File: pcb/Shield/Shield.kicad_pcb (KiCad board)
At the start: 2 copper layers, 17.8 x 33 mm, 30 parts, among them J11 TRRS_SJ1-42514, SW1 SW_RST, U1 ATMEGA32U4, X1 XTAL_GND

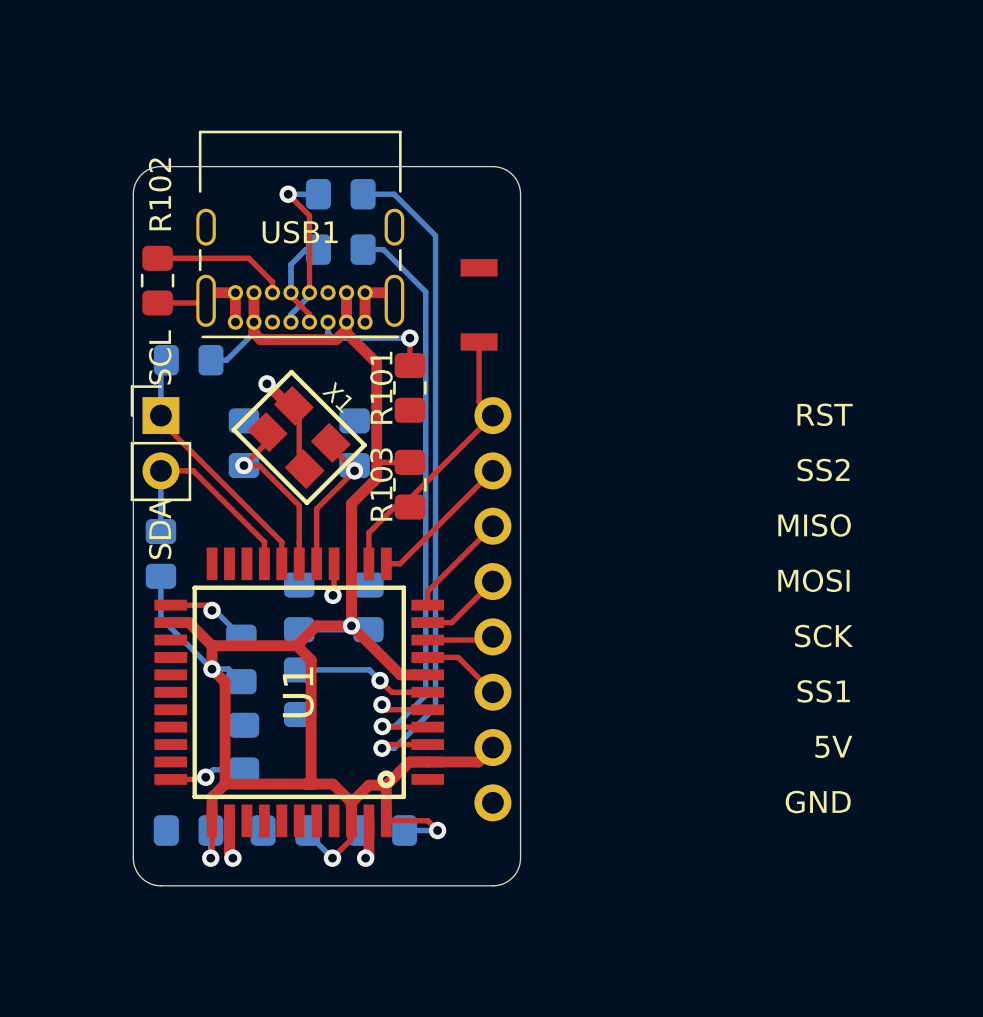
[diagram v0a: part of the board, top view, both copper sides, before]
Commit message: Modified shield to make i2c & usb connections solderless
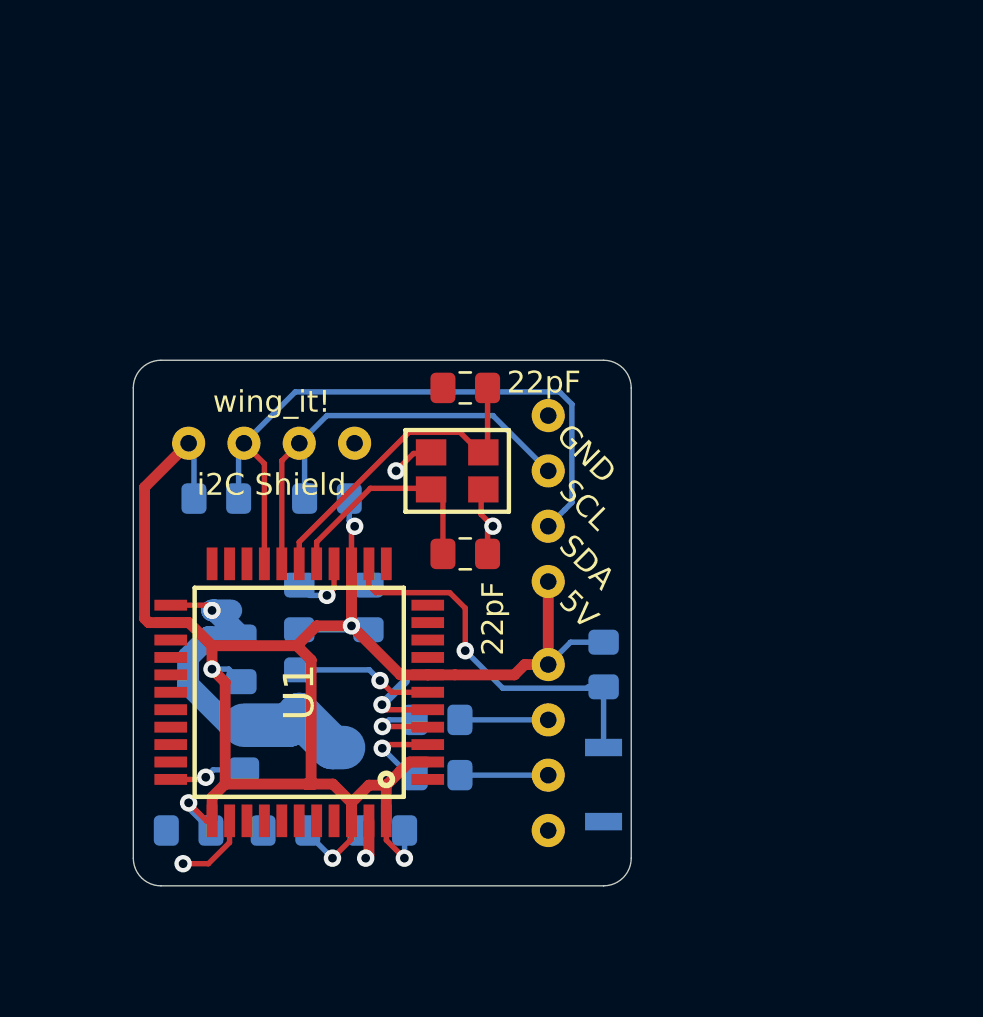
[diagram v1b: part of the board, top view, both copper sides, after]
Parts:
- removed GND, MISO, MOSI, RST, SCK, SS1, SS2, VCC: Conn_01x01, SVastaCustomParts:SinglePad
- removed J11: TRRS_SJ1-42514, Connector_PinHeader_2.54mm:PinHeader_1x02_P2.54mm_Vertical
- removed the R105 at (313.0, 44.6)
- removed the R106 at (304.7, 58.6)
- added I2C1: Conn_01x04_Female, SVastaCustomParts:Terminal_Block_4pos_On_Shore_Tech., F.Cu at (313.6, 53.5)
- added I2C2: Conn_01x04_Female, SVastaCustomParts:Terminal_Block_4pos_On_Shore_Tech., B.Cu at (322.5, 59.8)
- C108, C109: moved to F.Cu
- R101, R102: value 5.1K -> 22R; moved to B.Cu
- R103, SW1: moved to B.Cu
- R104: value 22 -> 4.7K
- USB1: value USB_C_Receptacle_USB2.0 -> Conn_01x04_Female; footprint Connector_USB:USB_C_Receptacle_GCT_USB4085 -> SVastaCustomParts:Terminal_Block_4pos_On_Shore_Tech.
- moved R102 26.1 mm to (317.4, 68.7), turned to 0 degrees
- moved USB1 24.8 mm to (322.5, 71.3), turned to 90 degrees
- moved SW1 22.7 mm to (325.0, 69.2), turned to 90 degrees
- moved R101 15.3 mm to (317.4, 66.2), turned to 0 degrees
- moved R104 15.1 mm to (307.2, 56.0)
- moved R103 12.1 mm to (325.0, 63.6)
- moved C109 10.5 mm to (318.7, 50.9), turned to 180 degrees
- moved R105 8.98 mm to (312.3, 56.0)
- moved X1 7.41 mm to (318.3, 54.8), turned to 0 degrees
- moved C108 7.18 mm to (318.7, 58.6), turned to 0 degrees
- renumbered R107 to R105, R108 to R106
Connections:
- R101 pad 1: GND -> /UsbD+
- R102 pad 1: GND -> /UsbD-
- R104 pad 1: Net-(R104-Pad1) -> SDA
- R104 pad 2: /UsbD- -> VCC
- U1 pad 3: Net-(R104-Pad1) -> /UsbD-
- U1 pad 4: Net-(R105-Pad1) -> /UsbD+
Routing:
- net Net-(R104-Pad1): track 31.2 -> 0.00 mm, vias 1 -> 0
- net Net-(R105-Pad1): track 26.9 -> 0.00 mm, vias 1 -> 0
- net SDA: track 9.88 -> 30.9 mm
- net GND: track 24.0 -> 36.9 mm, vias 6 -> 7
- net SCL: track 11.7 -> 21.5 mm
- net Net-(C109-Pad1): track 7.97 -> 15.0 mm, vias 1 -> 0
- net /SS2: track 6.66 -> 0.00 mm
- net VCC: track 95.2 -> 89.3 mm, vias 5 -> 6
- net /MISO: track 4.86 -> 0.00 mm
- net /RST: track 13.2 -> 17.7 mm, vias 0 -> 1
- net /UsbD-: track 8.02 -> 4.18 mm
- net /MOSI: track 3.77 -> 0.00 mm
- net Net-(C108-Pad1): track 6.81 -> 10.6 mm, vias 1 -> 0
- net /SS1: track 3.65 -> 0.00 mm
- net /SCK: track 3.05 -> 0.00 mm
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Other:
- board size 17.8 x 33 mm -> 22.9 x 24.1 mm
- board text added: "0.1uF"
- board text added: "10kR"
- board text added: "22R"
- board text added: "22pF"
- board text added: "4k7R"
- board text added: "4u7F"
- board text added: "D+"
- board text added: "D-"
- board text added: "i2C Shield"
- board text added: "wing_it!"
- board text removed: "MI"
- board text removed: "MISO"
- board text removed: "MO"
- board text removed: "MOSI"
- board text removed: "RST"
- board text removed: "SCK"
- board text removed: "SS1"
- board text removed: "SS2"
